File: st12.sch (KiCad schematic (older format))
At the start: 0 parts

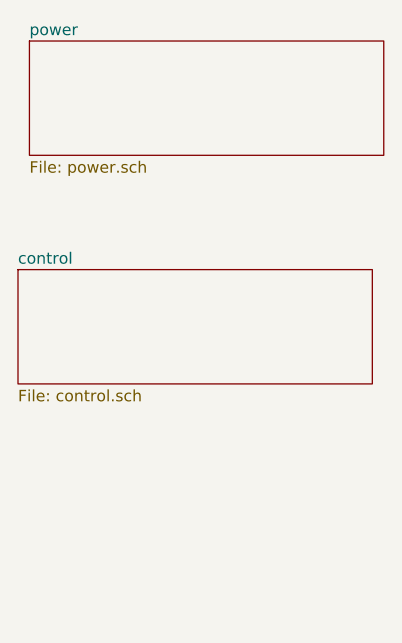
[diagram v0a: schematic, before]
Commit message: Fix ST12 schematics with current sensor (tested on balcony patch)
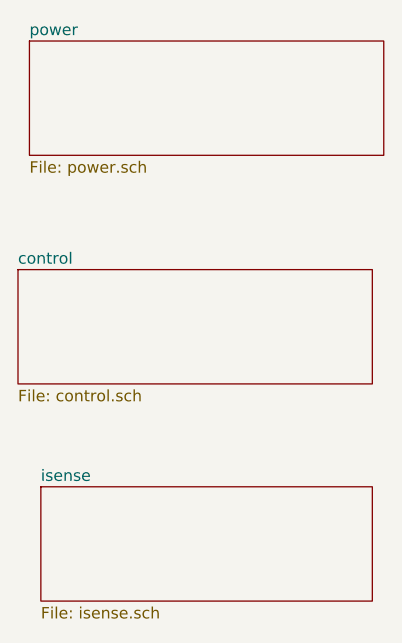
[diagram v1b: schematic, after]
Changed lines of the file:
@@
 $Descr A4 11693 8268
 encoding utf-8
-Sheet 1 3
+Sheet 1 4
 Title "T12 Soldering Station"
 Date "2021-05-16"
@@
 F1 "control.sch" 50
 $EndSheet
+$Sheet
+S 1050 2950 1450 500
+U 60C0CD20
+F0 "isense" 50
+F1 "isense.sch" 50
+$EndSheet
 $EndSCHEMATC
